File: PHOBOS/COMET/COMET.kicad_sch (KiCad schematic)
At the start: 80 parts, among them J2 M/D, J4 USB Boot, J5 Power/Arm, J6 USB_C_Receptacle_USB2.0_16P, Q1 SiSS63DN, Q2 BSD840N, Q3 SiSS63DN, SW1 SW_SPDT, SW3 KMR211GLFS, SW4 KMR211GLFS, U1 MPL3115A2, U2 LSM6DS3, U3 W25Q128JVSIQ, U4 NCP1117-3.3_SOT223, U5 RP2040, Y1 ABM8-272-T3

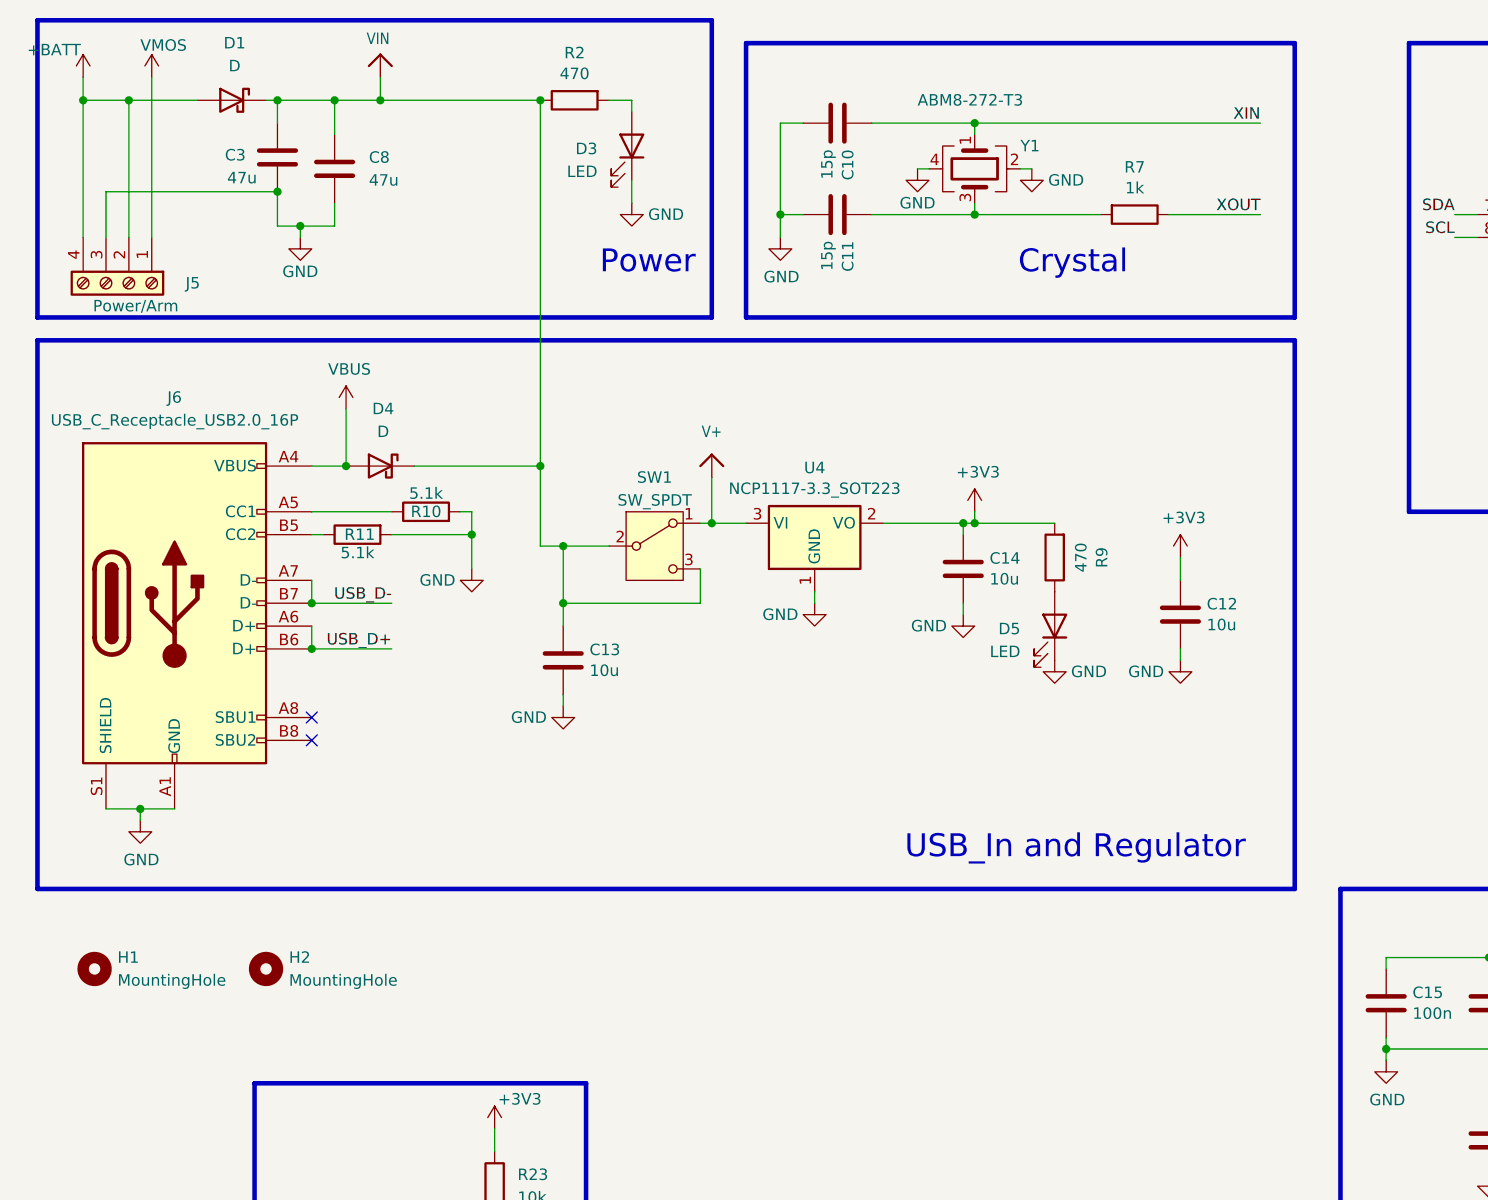
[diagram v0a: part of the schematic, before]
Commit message: USB updated, routed, added to BOM
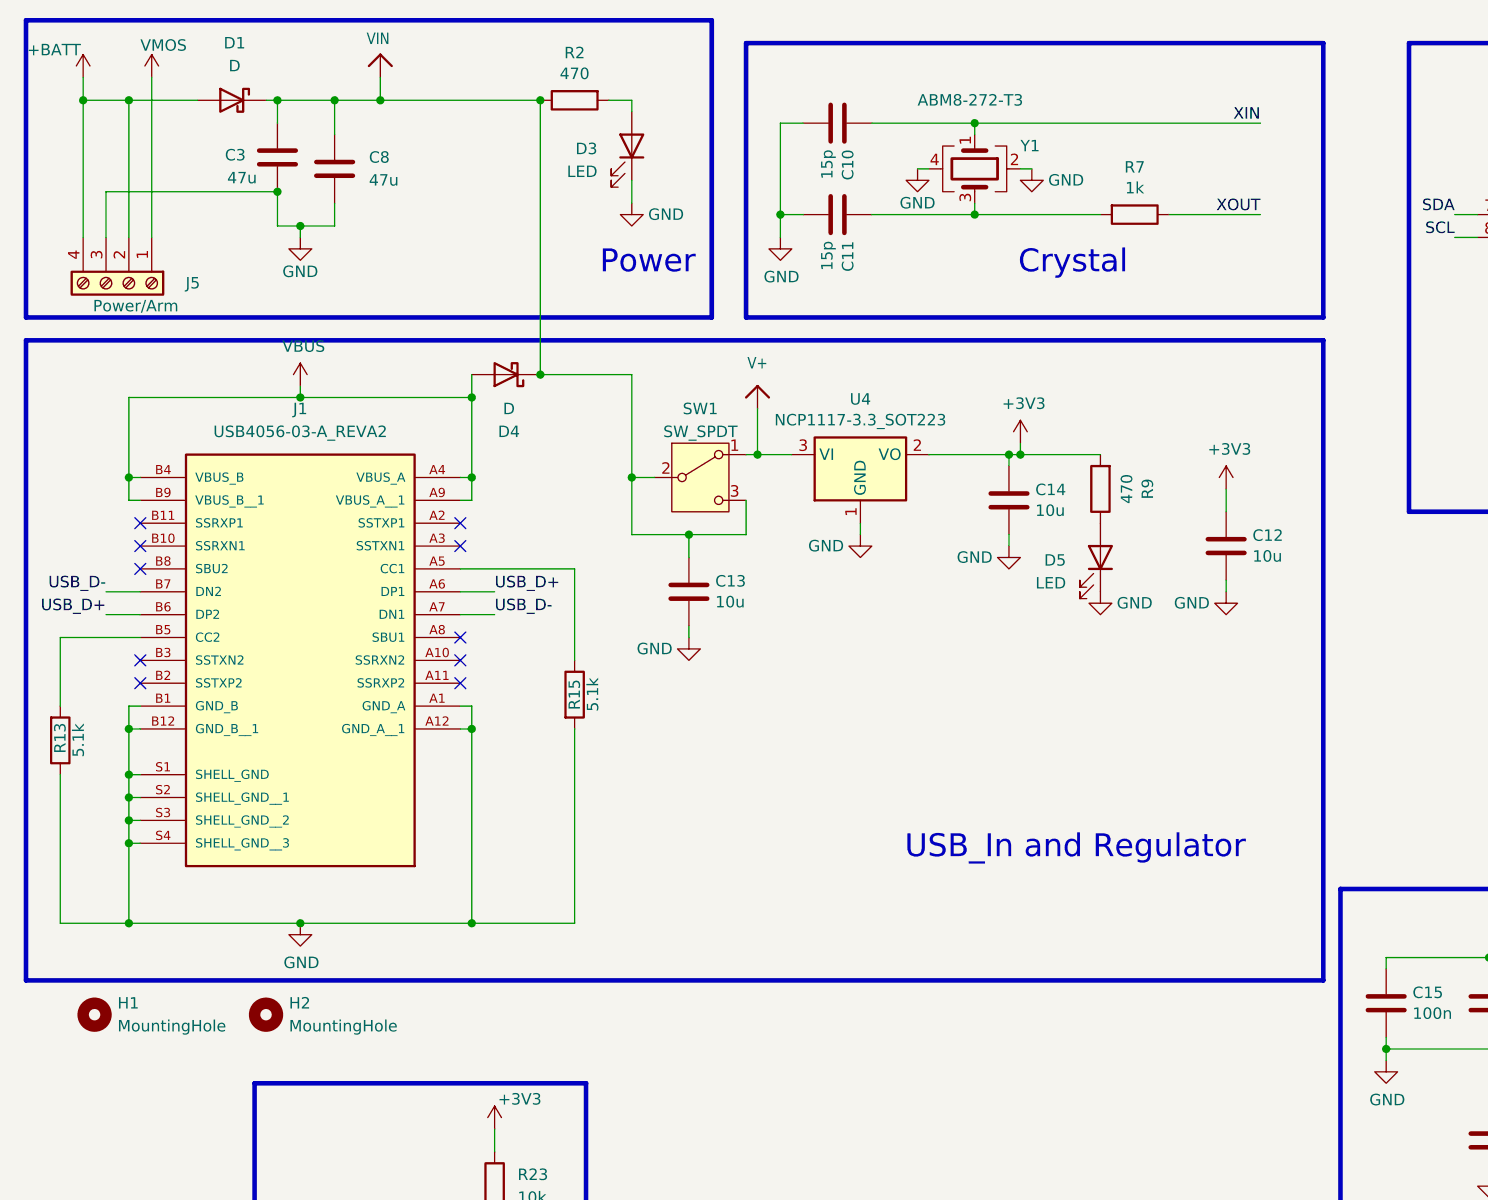
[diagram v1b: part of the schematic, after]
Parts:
- removed J6: USB_C_Receptacle_USB2.0_16P, External/Custom Parts:DX07S024JJ3R1300_JAE, symbol Connector:USB_C_Receptacle_USB2.0_16P
- removed R10, R11: 5.1k, Resistor_SMD:R_0402_1005Metric, symbol Device:R
- added J1: USB4056-03-A_REVA2, USB4056-03-A:GCT_USB4056-03-A_REVA2, symbol USB4056-03-A:USB4056-03-A_REVA2
- added R13, R15: 5.1k, Resistor_SMD:R_0402_1005Metric, symbol Device:R
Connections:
- net GND: now also J1.A1 (GND_A), J1.A12 (GND_A__1), J1.B1 (GND_B), J1.B12 (GND_B__1), J1.S1 (SHELL_GND), J1.S2 (SHELL_GND__1), J1.S3 (SHELL_GND__2), J1.S4 (SHELL_GND__3), R13.1, R15.2
- net USB_D+: now also J1.A6 (DP1), J1.B6 (DP2)
- net USB_D-: now also J1.A7 (DN1), J1.B7 (DN2)
- net VBUS: now also J1.A4 (VBUS_A), J1.A9 (VBUS_A__1), J1.B4 (VBUS_B), J1.B9 (VBUS_B__1)
- new net: J1.A5 (CC1), R15.1
- new net: J1.B5 (CC2), R13.2
- no-connect marks 12 -> 20
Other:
- moved on the sheet: C12, C13, C14, D4, D5, H1, H2, R9, SW1, U4

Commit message: BOM updated, Mosfets changed
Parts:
- Q2: value BSD840N -> PMGD175XNEX
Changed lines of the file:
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@@
 			)
 		)
-		(property "Value" "BSD840N"
+		(property "Value" "PMGD175XNEX"
 			(at 345.44 121.9199 0)
 			(show_name no)
@@
 			)
 		)
-		(property "Description" "BSD840N"
+		(property "Description" "PMGD175XNEX"
 			(at 339.09 120.65 0)
 			(hide yes)
@@
 			)
 		)
-		(property "Value" "BSD840N"
+		(property "Value" "PMGD175XNEX"
 			(at 345.44 176.5299 0)
 			(show_name no)
@@
 			)
 		)
-		(property "Description" "BSD840N"
+		(property "Description" "PMGD175XNEX"
 			(at 339.09 175.26 0)
 			(hide yes)

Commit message: Comet files reset. Mounting holes are currently centered.
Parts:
- removed J1: USB4056-03-A_REVA2, USB4056-03-A:GCT_USB4056-03-A_REVA2, symbol USB4056-03-A:USB4056-03-A_REVA2
- removed R13, R15: 5.1k, Resistor_SMD:R_0402_1005Metric, symbol Device:R
- removed SW1: SW_SPDT, External/Custom Parts:SWITCH_102AGRLC, symbol Switch:SW_SPDT
- added J6: USB4056-03-A_REVA2, USB4056-03-A:GCT_USB4056-03-A_REVA2, symbol USB4056-03-A:USB4056-03-A_REVA2
- added R10, R11: 5.1k, Resistor_SMD:R_0402_1005Metric, symbol Device:R
- added TP3: TX, TestPoint:TestPoint_THTPad_D2.0mm_Drill1.0mm, symbol Connector:TestPoint
- added TP4: RX, TestPoint:TestPoint_THTPad_D2.0mm_Drill1.0mm, symbol Connector:TestPoint
- C1, C15, C16, C17, C18, C19, C2, C20, C21, C22, C23, C9: MFG # (none) -> CL05B104KO5NNNC
- C10, C11: MFG # (none) -> GJM1555C1H150GB01D
- C12, C13, C14, C4: MFG # (none) -> CL10X106MO8NRNC
- C24, C25: MFG # (none) -> CL05A105KO5NNNC
- C3, C8: MFG # (none) -> MAL202135471E3; now left out of the parts list
- D1, D4: MFG # (none) -> CD0603-B0340R
- D10, D14: MFG # (none) -> QBLP601-IB5-S2897
- D13, D5, D9: MFG # (none) -> SML-D12U1WT86
- D15: MFG # (none) -> QBLP600L
- J2, J5: MFG # (none) -> A112370-ND
- LS1: footprint External/Custom Parts:OWMB-404020SA-40-17 -> Buzzer_Beeper:MagneticBuzzer_PUI_AT-0927-TT-6-R; MFG # (none) -> AT-0927-TT-6-R
- Q1, Q3: value SiSS63DN -> SISS67DN-T1-GE3; MFG # (none) -> SISS67DN-T1-GE3
- Q2: value PMGD175XNEX -> BSD840N; MFG # (none) -> PMGD175XNEX
- R12, R23, R24, R31: MFG # (none) -> AC0402FR-7W10KL
- R14, R22, R9: MFG # (none) -> AC0402FR-7W470RL
- R16, R28: MFG # (none) -> AC0402FR-7W220RL
- R17, R29, R33, R34, R35, R7: MFG # (none) -> AC0402FR-7W1KL
- R18, R25, R26, R30: MFG # (none) -> AC0402FR-7W4K7L
- R19, R21: MFG # (none) -> RC0402FR-7W27RL
- R32: MFG # (none) -> AC0402FR-7W10KL; now left out of the parts list
- R36: MFG # (none) -> CRGCQ0402F330K
- R37: MFG # (none) -> AC0402FR-7W100KL
- R6: MFG # (none) -> AC0402FR-7W1KL; now left out of the parts list
- SW3: MFG # (none) -> KMR211G LFS
- SW4: MFG # (none) -> KMR211G LFS; now left out of the parts list
- TP1, TP2: now left out of the parts list
- U1: MFG # (none) -> MPL3115A2ST1
- U2: MFG # (none) -> LSM6DSO32TR
- U3: MFG # (none) -> Winbond W25Q128JVSIQ
- U4: MFG # (none) -> NCP1117ST33T3G
- U5: MFG # (none) -> SC0914(13)
- Y1: MFG # (none) -> ABM8-272-T3
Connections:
- net VIN is gone; now on net V+: C13.1, C3.1, C8.1, D1.1 (K), D4.1 (K), R2.1
- net +BATT: no longer D1.2 (A)
- net GND: now also J6.A1 (GND_A), J6.A12 (GND_A__1), J6.B1 (GND_B), J6.B12 (GND_B__1), J6.S1 (SHELL_GND), J6.S2 (SHELL_GND__1), J6.S3 (SHELL_GND__2), J6.S4 (SHELL_GND__3), R10.2, R11.1
- net RX: now also TP4.1
- net TX: now also TP3.1
- net USB_D+: now also J6.A6 (DP1), J6.B6 (DP2)
- net USB_D-: now also J6.A7 (DN1), J6.B7 (DN2)
- net VBUS: now also J6.A4 (VBUS_A), J6.A9 (VBUS_A__1), J6.B4 (VBUS_B), J6.B9 (VBUS_B__1)
- net VMOS: now also D1.2 (A)
- new net: J6.A5 (CC1), R10.1
- new net: J6.B5 (CC2), R11.2
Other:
- note added: "Dont need current limiting to gate because of <-"
- note removed: "Doesnt require current limiting because R17/9"
- moved on the sheet: C12, C13, C14, D5, H1, H2, R23, R9, TP1, TP2, U4

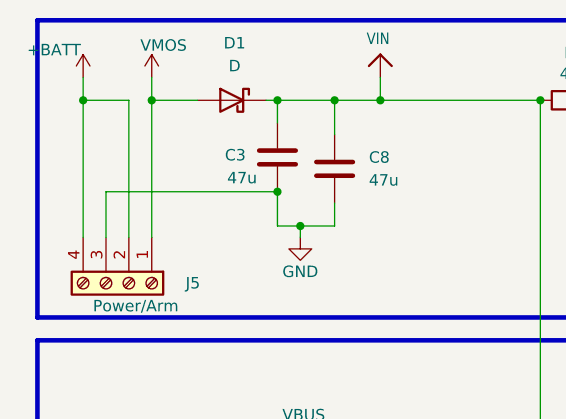
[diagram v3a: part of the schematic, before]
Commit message: Arming is back. VMOS now does not break power to board
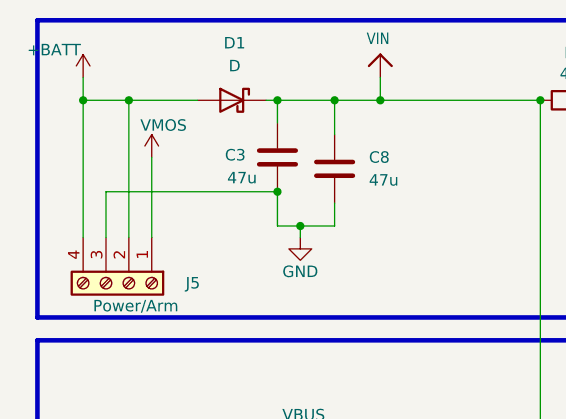
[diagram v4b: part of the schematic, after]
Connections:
- net +BATT: now also D1.2 (A)
- net VMOS: no longer D1.2 (A)
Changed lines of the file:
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@@
 	)
 	(junction
+		(at 24.13 21.59)
+		(diameter 0)
+		(color 0 0 0 0)
+	)
+	(junction
 		(at 83.82 68.58)
 		(diameter 0)
@@
 	)
 	(junction
-		(at 26.67 21.59)
-		(diameter 0)
-		(color 0 0 0 0)
-	)
-	(junction
 		(at 96.52 34.29)
 		(diameter 0)
@@
 	(wire
 		(pts
+			(xy 26.67 27.94) (xy 26.67 36.83)
+		)
+		(stroke
+			(width 0)
+			(type default)
+		)
+	)
+	(wire
+		(pts
 			(xy 99.06 34.29) (xy 96.52 34.29)
 		)
@@
 	(wire
 		(pts
-			(xy 26.67 21.59) (xy 26.67 36.83)
-		)
-		(stroke
-			(width 0)
-			(type default)
-		)
-	)
-	(wire
-		(pts
 			(xy 275.59 163.83) (xy 279.4 163.83)
 		)
@@
 	(wire
 		(pts
-			(xy 26.67 19.05) (xy 26.67 21.59)
-		)
-		(stroke
-			(width 0)
-			(type default)
-		)
-	)
-	(wire
-		(pts
 			(xy 191.77 251.46) (xy 191.77 254)
 		)
@@
 	(wire
 		(pts
-			(xy 26.67 21.59) (xy 31.75 21.59)
+			(xy 24.13 21.59) (xy 31.75 21.59)
 		)
 		(stroke
@@
 	)
 	(symbol
-		(lib_id "power:+3V3")
-		(at 387.35 104.14 0)
+		(lib_id "power:VCC")
+		(at 26.67 27.94 0)
 		(unit 1)
 		(body_style 1)
@@
 		(in_pos_files yes)
 		(dnp no)
-		(property "Reference" "#PWR027"
-			(at 387.35 107.95 0)
+		(property "Reference" "#PWR026"
+			(at 26.67 31.75 0)
 			(hide yes)
 			(show_name no)
@@
 			)
 		)
-		(property "Value" "+3V3"
-			(at 387.731 99.7458 0)
+		(property "Value" "VMOS"
+			(at 25.4 24.384 0)
 			(show_name no)
 			(do_not_autoplace no)
@@
 					(size 1.27 1.27)
 				)
+				(justify left)
 			)
 		)
 		(property "Footprint" ""
-			(at 387.35 104.14 0)
+			(at 26.67 27.94 0)
 			(hide yes)
 			(show_name no)
@@
 		)
 		(property "Datasheet" ""
-			(at 387.35 104.14 0)
+			(at 26.67 27.94 0)
 			(hide yes)
 			(show_name no)
@@
 			)
 		)
-		(property "Description" ""
-			(at 387.35 104.14 0)
+		(property "Description" "Power symbol creates a global label with name \"VCC\""
+			(at 26.67 27.94 0)
 			(hide yes)
 			(show_name no)
@@
 			(project "COMET"
 				(path "/bf4b749c-e7df-4d18-856a-a4f784e96f1a"
-					(reference "#PWR027")
+					(reference "#PWR026")
 					(unit 1)
 				)
@@
 	)
 	(symbol
-		(lib_id "power:VCC")
-		(at 26.67 19.05 0)
+		(lib_id "power:+3V3")
+		(at 387.35 104.14 0)
 		(unit 1)
 		(body_style 1)
@@
 		(in_pos_files yes)
 		(dnp no)
-		(property "Reference" "#PWR026"
-			(at 26.67 22.86 0)
+		(property "Reference" "#PWR027"
+			(at 387.35 107.95 0)
 			(hide yes)
 			(show_name no)
@@
 			)
 		)
-		(property "Value" "VMOS"
-			(at 25.4 15.494 0)
+		(property "Value" "+3V3"
+			(at 387.731 99.7458 0)
 			(show_name no)
 			(do_not_autoplace no)
@@
 					(size 1.27 1.27)
 				)
-				(justify left)
 			)
 		)
 		(property "Footprint" ""
-			(at 26.67 19.05 0)
+			(at 387.35 104.14 0)
 			(hide yes)
 			(show_name no)
@@
 		)
 		(property "Datasheet" ""
-			(at 26.67 19.05 0)
+			(at 387.35 104.14 0)
 			(hide yes)
 			(show_name no)
@@
 			)
 		)
-		(property "Description" "Power symbol creates a global label with name \"VCC\""
-			(at 26.67 19.05 0)
+		(property "Description" ""
+			(at 387.35 104.14 0)
 			(hide yes)
 			(show_name no)
@@
 			(project "COMET"
 				(path "/bf4b749c-e7df-4d18-856a-a4f784e96f1a"
-					(reference "#PWR026")
+					(reference "#PWR027")
 					(unit 1)
 				)

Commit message: board settings updated from PHOBOS. Stackup now matches all advanced PCB requirements. Net classes added for the current traces
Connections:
- net V+ renamed VIN
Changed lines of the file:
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@@
 	)
 	(junction
-		(at 88.9 68.58)
-		(diameter 0)
-		(color 0 0 0 0)
-	)
-	(junction
 		(at 341.63 170.18)
 		(diameter 0)
@@
 	(wire
 		(pts
-			(xy 88.9 68.58) (xy 92.71 68.58)
-		)
-		(stroke
-			(width 0)
-			(type default)
-		)
-	)
-	(wire
-		(pts
 			(xy 314.96 193.04) (xy 314.96 191.77)
 		)
@@
 	(wire
 		(pts
-			(xy 88.9 63.5) (xy 88.9 68.58)
-		)
-		(stroke
-			(width 0)
-			(type default)
-		)
-	)
-	(wire
-		(pts
 			(xy 262.89 22.86) (xy 240.03 22.86)
 		)
@@
 	(wire
 		(pts
-			(xy 88.9 68.58) (xy 83.82 68.58)
+			(xy 83.82 68.58) (xy 92.71 68.58)
 		)
 		(stroke
@@
 		)
 	)
+	(netclass_flag ""
+		(length 2.54)
+		(shape round)
+		(at 356.87 104.14 0)
+		(fields_autoplaced yes)
+		(effects
+			(font
+				(size 1.27 1.27)
+			)
+			(justify left bottom)
+		)
+		(property "Netclass" "Current"
+			(at 357.5685 101.6 0)
+			(show_name no)
+			(do_not_autoplace no)
+			(effects
+				(font
+					(size 1.27 1.27)
+				)
+				(justify left)
+			)
+		)
+		(property "Component Class" ""
+			(at -62.23 7.62 0)
+			(show_name no)
+			(do_not_autoplace no)
+			(effects
+				(font
+					(size 1.27 1.27)
+					(italic yes)
+				)
+			)
+		)
+	)
+	(netclass_flag ""
+		(length 2.54)
+		(shape round)
+		(at 21.59 21.59 0)
+		(fields_autoplaced yes)
+		(effects
+			(font
+				(size 1.27 1.27)
+			)
+			(justify left bottom)
+		)
+		(property "Netclass" "Current"
+			(at 22.2885 19.05 0)
+			(show_name no)
+			(do_not_autoplace no)
+			(effects
+				(font
+					(size 1.27 1.27)
+				)
+				(justify left)
+			)
+		)
+		(property "Component Class" ""
+			(at -397.51 -74.93 0)
+			(show_name no)
+			(do_not_autoplace no)
+			(effects
+				(font
+					(size 1.27 1.27)
+					(italic yes)
+				)
+			)
+		)
+	)
 	(symbol
 		(lib_id "MCU_RaspberryPi_RP2040:RP2040")
@@
 					(unit 1)
 				)
-			)
-		)
-	)
-	(symbol
-		(lib_id "Adafruit MPM3610-eagle-import:VIN")
-		(at 88.9 60.96 0)
-		(unit 1)
-		(body_style 1)
-		(exclude_from_sim no)
-		(in_bom yes)
-		(on_board yes)
-		(in_pos_files yes)
-		(dnp no)
-		(fields_autoplaced yes)
-		(property "Reference" "#U$02"
-			(at 88.9 60.96 0)
-			(hide yes)
-			(show_name no)
-			(do_not_autoplace no)
-			(effects
-				(font
-					(size 1.27 1.27)
-				)
-			)
-		)
-		(property "Value" "V+"
-			(at 88.9 58.42 0)
-			(show_name no)
-			(do_not_autoplace no)
-			(effects
-				(font
-					(size 1.27 1.0795)
-				)
-			)
-		)
-		(property "Footprint" ""
-			(at 88.9 60.96 0)
-			(hide yes)
-			(show_name no)
-			(do_not_autoplace no)
-			(effects
-				(font
-					(size 1.27 1.27)
-				)
-			)
-		)
-		(property "Datasheet" ""
-			(at 88.9 60.96 0)
-			(hide yes)
-			(show_name no)
-			(do_not_autoplace no)
-			(effects
-				(font
-					(size 1.27 1.27)
-				)
-			)
-		)
-		(property "Description" ""
-			(at 88.9 60.96 0)
-			(hide yes)
-			(show_name no)
-			(do_not_autoplace no)
-			(effects
-				(font
-					(size 1.27 1.27)
-				)
-			)
-		)
-		(pin "1"
-		)
-		(instances
-			(project "COMET"
-				(path "/bf4b749c-e7df-4d18-856a-a4f784e96f1a"
-					(reference "#U$02")
-					(unit 1)
-				)

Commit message: Speaker repositioned
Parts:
- LS1: footprint Buzzer_Beeper:MagneticBuzzer_PUI_AT-0927-TT-6-R -> OWMB-404020SA-40-17:OWMB-404020SA-40-17
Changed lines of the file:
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@@
 			)
 		)
-		(property "Footprint" "Buzzer_Beeper:MagneticBuzzer_PUI_AT-0927-TT-6-R"
+		(property "Footprint" "OWMB-404020SA-40-17:OWMB-404020SA-40-17"
 			(at 267.97 191.77 0)
 			(hide yes)
